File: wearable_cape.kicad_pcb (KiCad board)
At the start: 2 copper layers, 70.5 x 54.6 mm, 51 parts, among them P1 BELA_AINS, P2 RECEIVER, P3 BATTERY, P4 BELA_AOUTS, P5 CONN_01X04, P6 CONN_01X04, P7 CONN_01X04, SW1 SW_HALT, SW2 SW_MODE_SEL, U1 MCP6004, U2 MCP6004, U3 BEAGLEBONEBLACK, U4 OKI_7805

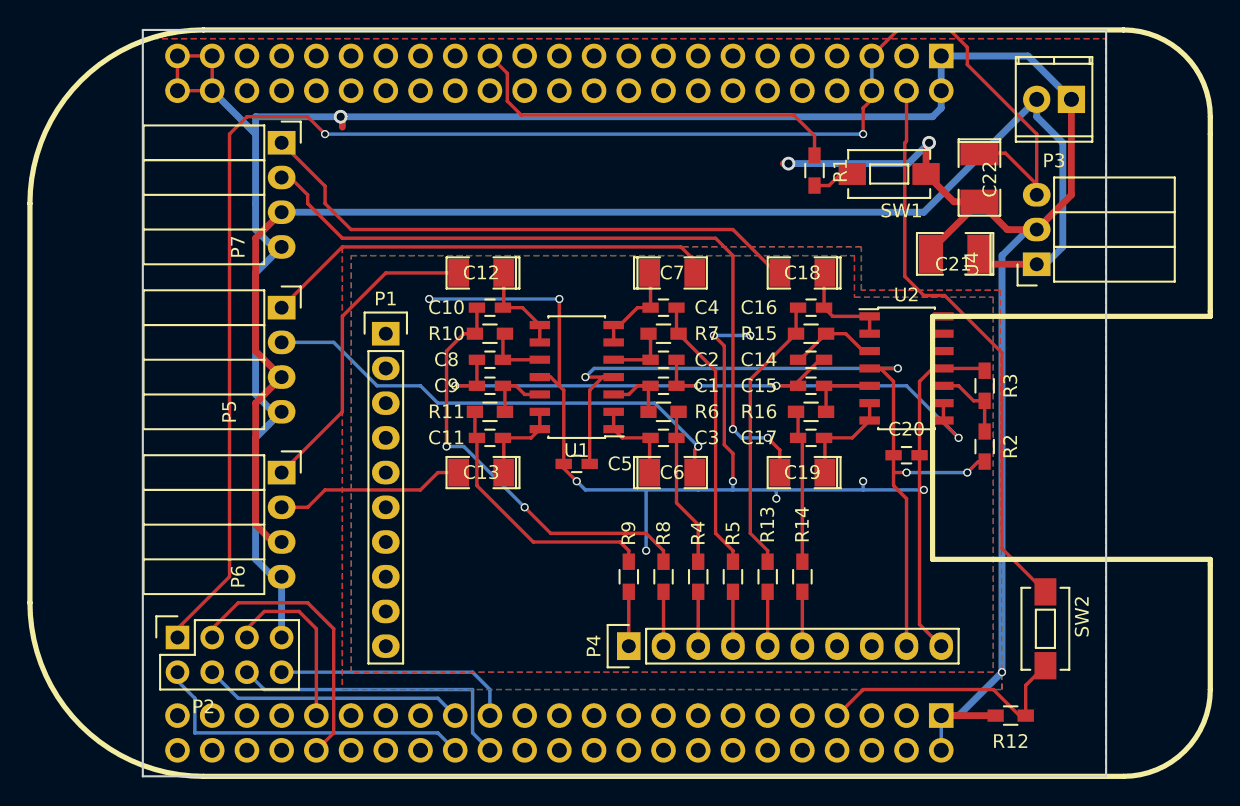
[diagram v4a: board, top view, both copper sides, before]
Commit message: updates to pcb: add attenuation, add headphone jacks, fix power supply opamps
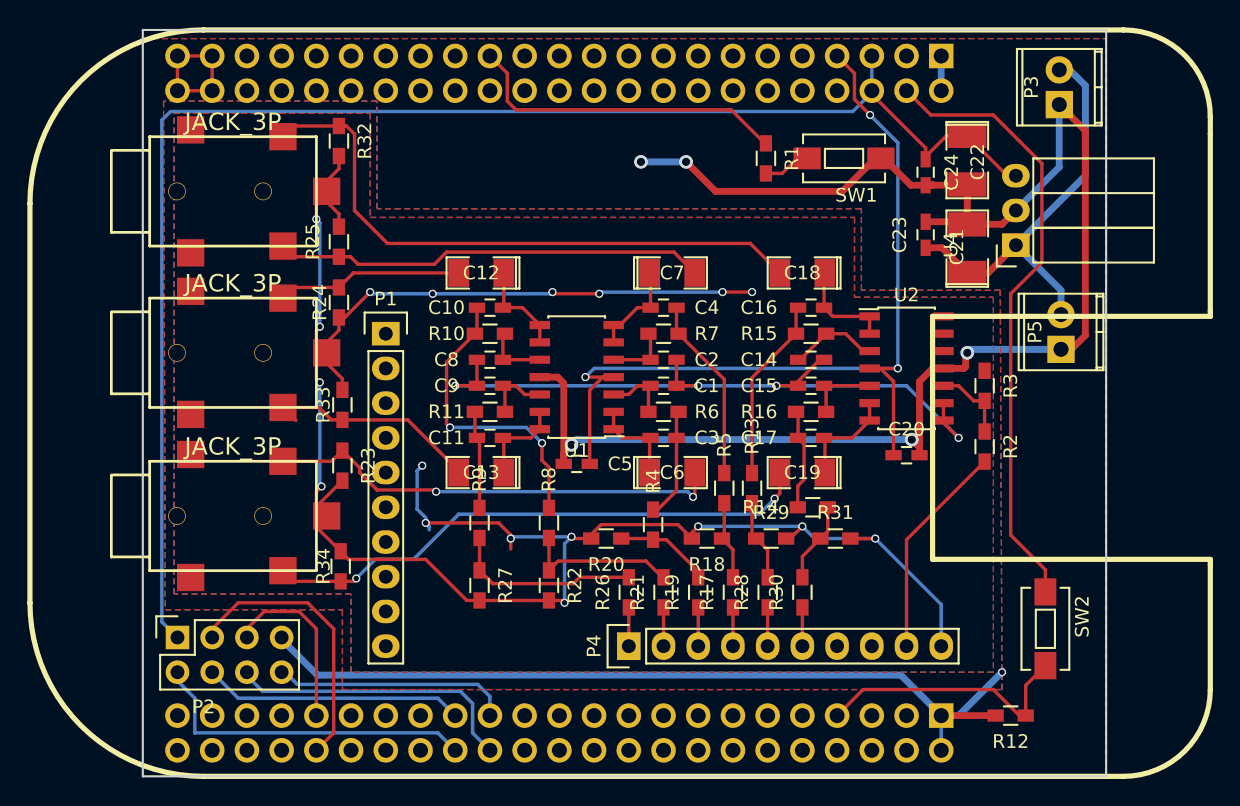
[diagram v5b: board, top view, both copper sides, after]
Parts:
- removed P6, P7: CONN_01X04, Socket_Strips:Socket_Strip_Angled_1x04
- added C23: C, Capacitors_SMD:C_0603_HandSoldering, F.Cu at (89.0, 33.4)
- added C24: C, Capacitors_SMD:C_0603_HandSoldering, F.Cu at (89.0, 28.8)
- added J1: JACK_3P, Lumberg:Lumberg_1503_03, F.Cu at (38.4, 54.0)
- added J2: JACK_3P, Lumberg:Lumberg_1503_03, F.Cu at (38.4, 42.0)
- added J3: JACK_3P, Lumberg:Lumberg_1503_03, F.Cu at (38.4, 30.2)
- added R17: 150k, Resistors_SMD:R_0603_HandSoldering, F.Cu at (74.9, 59.6)
- added R18: 200k, Resistors_SMD:R_0603_HandSoldering, F.Cu at (73.0, 55.6)
- added R19: 150k, Resistors_SMD:R_0603_HandSoldering, F.Cu at (72.4, 59.6)
- added R20: 200k, Resistors_SMD:R_0603_HandSoldering, F.Cu at (65.7, 55.6)
- added R21: 150k, Resistors_SMD:R_0603_HandSoldering, F.Cu at (69.8, 59.6)
- added R22: 200k, Resistors_SMD:R_0603_HandSoldering, F.Cu at (61.5, 59.1)
- added R23: 100k, Resistors_SMD:R_0603_HandSoldering, F.Cu at (46.4, 50.3)
- added R24: 100k, Resistors_SMD:R_0603_HandSoldering, F.Cu at (46.1, 38.4)
- added R25: 100k, Resistors_SMD:R_0603_HandSoldering, F.Cu at (46.1, 33.9)
- added R26: 150k, Resistors_SMD:R_0603_HandSoldering, F.Cu at (67.3, 59.6)
- added R27: 200k, Resistors_SMD:R_0603_HandSoldering, F.Cu at (56.4, 59.1)
- added R28: 150k, Resistors_SMD:R_0603_HandSoldering, F.Cu at (77.5, 59.6)
- added R29: 200k, Resistors_SMD:R_0603_HandSoldering, F.Cu at (77.7, 55.6)
- added R30: 150k, Resistors_SMD:R_0603_HandSoldering, F.Cu at (80.0, 59.6)
- added R31: 200k, Resistors_SMD:R_0603_HandSoldering, F.Cu at (82.4, 55.6)
- added R32: 100k, Resistors_SMD:R_0603_HandSoldering, F.Cu at (46.1, 26.5)
- added R33: 100k, Resistors_SMD:R_0603_HandSoldering, F.Cu at (46.4, 45.8)
- added R34: 100k, Resistors_SMD:R_0603_HandSoldering, F.Cu at (46.2, 57.7)
- P5: value CONN_01X04 -> PWR_OUT; footprint Socket_Strips:Socket_Strip_Angled_1x04 -> Terminal_Blocks:TerminalBlock_Pheonix_MPT-2.54mm_2pol
- moved P5 57.1 mm to (98.9, 41.8), turned to 90 degrees
- moved R9 11.6 mm to (56.4, 54.5)
- moved R8 9.26 mm to (61.5, 54.5)
- moved R13 6.58 mm to (76.3, 51.9)
- moved R5 6.51 mm to (74.3, 51.9)
- moved R14 5.14 mm to (80.8, 53.3), turned to 0 degrees
- moved R4 5.04 mm to (69.1, 54.6)
- moved R1 3.67 mm to (77.3, 27.8)
- moved SW1 3.49 mm to (83.1, 27.8)
- moved U4 2.07 mm to (95.6, 34.2)
- moved C22 1.55 mm to (92.1, 27.9)
- moved C21 0.97 mm to (92.1, 34.4), turned to 90 degrees
- moved P3 0.97 mm to (98.8, 23.9), turned to 90 degrees
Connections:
- C20 pad 1: VCC -> SYS_5V
- C20 pad 2: GNDA -> GND
- C5 pad 1: VCC -> SYS_5V
- C5 pad 2: GNDA -> GND
- P5 pad 1: /FILT_OUT1 -> GND
- P5 pad 2: /FILT_OUT0 -> BAT_11.1V
- R13 pad 2: /BELA_OUT4 -> Net-(R13-Pad2)
- R14 pad 2: /BELA_OUT5 -> Net-(R14-Pad2)
- R4 pad 2: /BELA_OUT2 -> Net-(R19-Pad2)
- R5 pad 2: /BELA_OUT3 -> Net-(R17-Pad2)
- R8 pad 2: /BELA_OUT1 -> Net-(R21-Pad2)
- R9 pad 2: /BELA_OUT0 -> Net-(R26-Pad2)
- U1 pad 11: GNDA -> GND
- U1 pad 4: VCC -> SYS_5V
- U2 pad 11: GNDA -> GND
- U2 pad 4: VCC -> SYS_5V
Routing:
- net BAT_11.1V: track 105.5 -> 30.8 mm
- net SYS_5V: track 0.00 -> 67.0 mm, vias 0 -> 3
- net GNDA: track 96.6 -> 153.7 mm, vias 10 -> 18
- net VCC: track 63.7 -> 15.9 mm, vias 4 -> 0
- net Net-(R26-Pad2): track 0.00 -> 13.9 mm
- net GND: track 209.7 -> 196.0 mm, vias 4 -> 6
- net /FILT_OUT5: track 54.2 -> 41.0 mm
- net Net-(C11-Pad2): track 19.3 -> 7.17 mm
- net Net-(R21-Pad2): track 0.00 -> 11.5 mm
- net RAW_5V: track 118.9 -> 109.1 mm, vias 2 -> 0
- net /FILT_OUT2: track 23.1 -> 13.6 mm
- net Net-(C10-Pad2): track 31.4 -> 21.9 mm
- net Net-(C16-Pad2): track 20.6 -> 13.5 mm
- net Net-(R19-Pad2): track 0.00 -> 7.05 mm
- net Net-(C4-Pad2): track 20.3 -> 13.6 mm
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
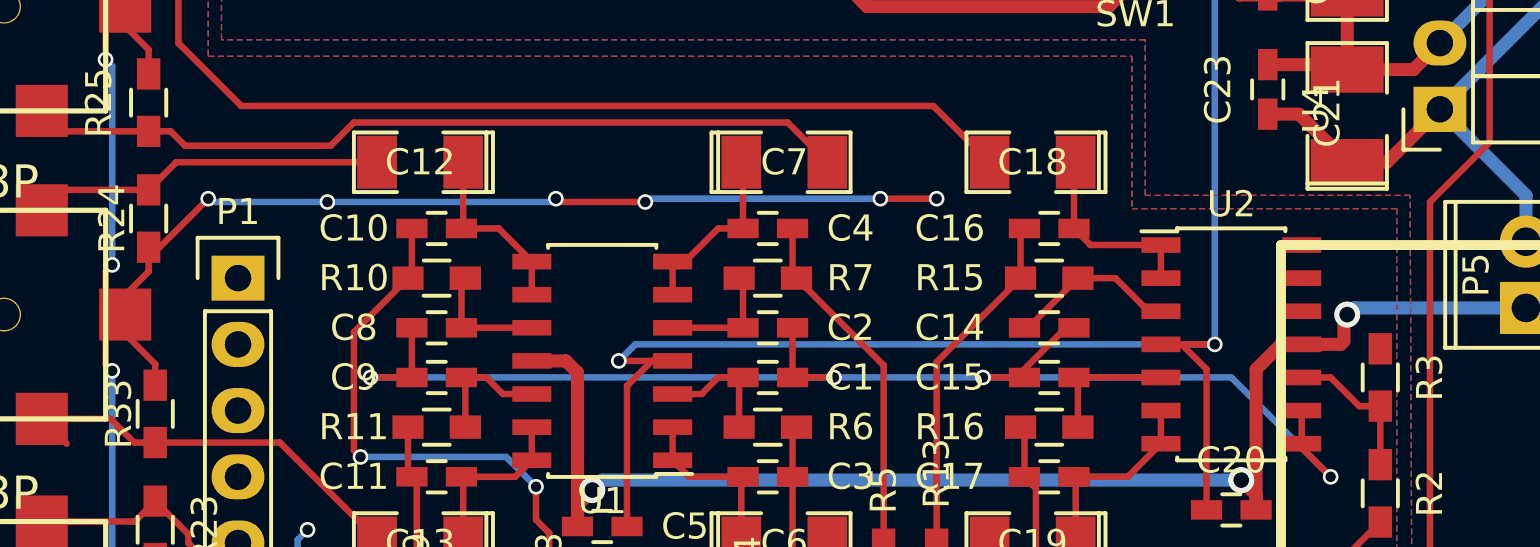
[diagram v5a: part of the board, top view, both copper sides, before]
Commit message: small update to pcb, updates to BOM
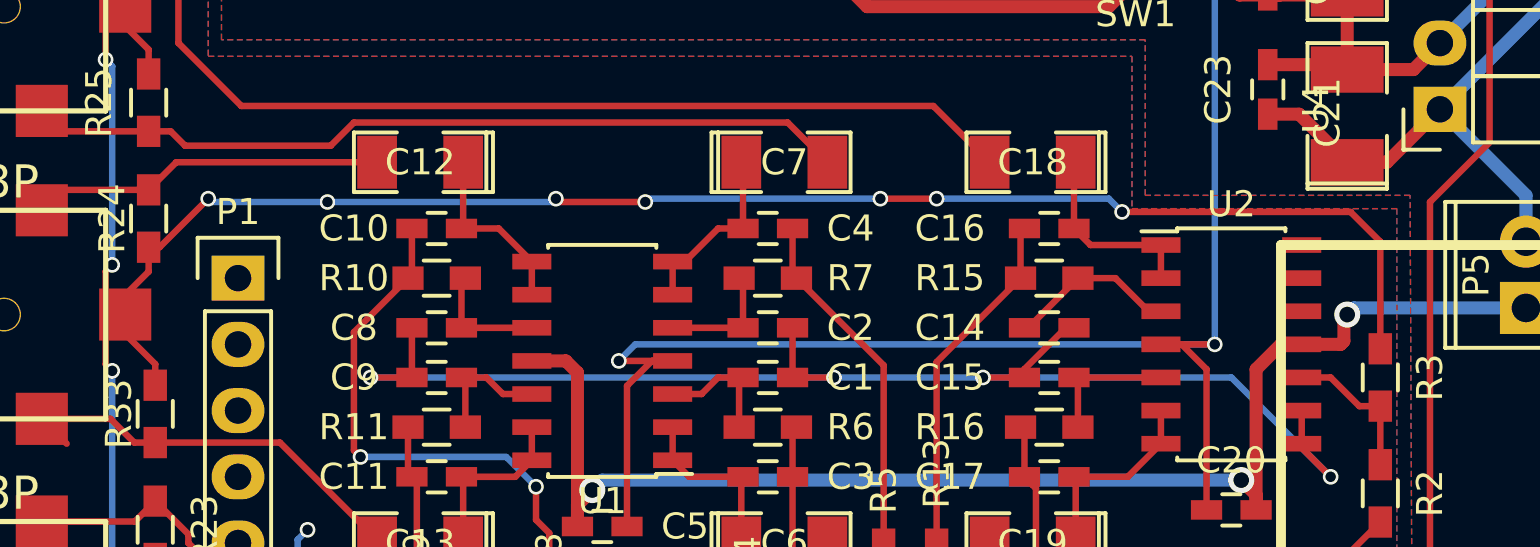
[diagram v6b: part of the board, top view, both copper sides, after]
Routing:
- net GNDA: track 153.7 -> 175.5 mm, vias 18 -> 19
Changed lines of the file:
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@@
   (general
     (links 143)
-    (no_connects 1)
-    (area 31.674999 18.339999 102.310001 73.100001)
+    (no_connects 0)
+    (area 23.004499 17.924499 110.345501 73.515501)
     (thickness 1.6)
     (drawings 4)
-    (tracks 464)
+    (tracks 470)
     (zones 0)
     (modules 72)
@@
   (segment (start 43.18 60.96) (end 44.45 62.23) (width 0.25) (layer F.Cu) (net 121))
   (segment (start 44.45 62.23) (end 44.45 68.58) (width 0.25) (layer F.Cu) (net 121))
-  (segment (start 52.959 37.719) (end 61.595 37.719) (width 0.25) (layer B.Cu) (net 122))
-  (via (at 48.387 37.592) (size 0.6) (drill 0.4) (layers F.Cu B.Cu) (net 122))
-  (segment (start 48.387 37.592) (end 48.514 37.719) (width 0.25) (layer B.Cu) (net 122))
-  (segment (start 48.514 37.719) (end 52.959 37.719) (width 0.25) (layer B.Cu) (net 122))
-  (via (at 52.959 37.719) (size 0.6) (drill 0.4) (layers F.Cu B.Cu) (net 122))
-  (segment (start 46.525 39.454) (end 48.387 37.592) (width 0.25) (layer F.Cu) (net 122))
-  (via (at 76.327 37.592) (size 0.6) (drill 0.4) (layers F.Cu B.Cu) (net 122))
-  (segment (start 74.168 37.592) (end 76.327 37.592) (width 0.25) (layer F.Cu) (net 122))
-  (via (at 74.168 37.592) (size 0.6) (drill 0.4) (layers F.Cu B.Cu) (net 122))
-  (segment (start 65.278 37.592) (end 74.168 37.592) (width 0.25) (layer B.Cu) (net 122))
-  (segment (start 65.151 37.719) (end 65.278 37.592) (width 0.25) (layer B.Cu) (net 122))
-  (via (at 65.151 37.719) (size 0.6) (drill 0.4) (layers F.Cu B.Cu) (net 122))
-  (segment (start 61.849 37.719) (end 65.151 37.719) (width 0.25) (layer F.Cu) (net 122))
-  (segment (start 61.722 37.592) (end 61.849 37.719) (width 0.25) (layer F.Cu) (net 122))
-  (via (at 61.722 37.592) (size 0.6) (drill 0.4) (layers F.Cu B.Cu) (net 122))
+  (segment (start 93.345 43.35) (end 93.345 39.243) (width 0.25) (layer F.Cu) (net 122) (status 400000))
   (segment (start 61.595 37.719) (end 61.722 37.592) (width 0.25) (layer B.Cu) (net 122))
+  (via (at 61.722 37.592) (size 0.6) (drill 0.4) (layers F.Cu B.Cu) (net 122))
+  (segment (start 61.722 37.592) (end 61.849 37.719) (width 0.25) (layer F.Cu) (net 122))
+  (segment (start 61.849 37.719) (end 65.151 37.719) (width 0.25) (layer F.Cu) (net 122))
+  (via (at 65.151 37.719) (size 0.6) (drill 0.4) (layers F.Cu B.Cu) (net 122))
+  (segment (start 65.151 37.719) (end 65.278 37.592) (width 0.25) (layer B.Cu) (net 122))
+  (segment (start 65.278 37.592) (end 74.168 37.592) (width 0.25) (layer B.Cu) (net 122))
+  (via (at 74.168 37.592) (size 0.6) (drill 0.4) (layers F.Cu B.Cu) (net 122))
+  (segment (start 74.168 37.592) (end 76.327 37.592) (width 0.25) (layer F.Cu) (net 122))
+  (via (at 76.327 37.592) (size 0.6) (drill 0.4) (layers F.Cu B.Cu) (net 122))
+  (segment (start 48.387 37.592) (end 46.525 39.454) (width 0.25) (layer F.Cu) (net 122))
+  (via (at 52.959 37.719) (size 0.6) (drill 0.4) (layers F.Cu B.Cu) (net 122))
+  (segment (start 48.514 37.719) (end 52.959 37.719) (width 0.25) (layer B.Cu) (net 122))
+  (segment (start 48.387 37.592) (end 48.514 37.719) (width 0.25) (layer B.Cu) (net 122))
+  (via (at 48.387 37.592) (size 0.6) (drill 0.4) (layers F.Cu B.Cu) (net 122))
+  (segment (start 52.959 37.719) (end 61.595 37.719) (width 0.25) (layer B.Cu) (net 122))
+  (segment (start 82.931 37.592) (end 76.327 37.592) (width 0.25) (layer B.Cu) (net 122))
+  (segment (start 83.439 38.1) (end 82.931 37.592) (width 0.25) (layer B.Cu) (net 122))
+  (via (at 83.439 38.1) (size 0.6) (drill 0.4) (layers F.Cu B.Cu) (net 122))
+  (segment (start 92.202 38.1) (end 83.439 38.1) (width 0.25) (layer F.Cu) (net 122))
+  (segment (start 93.345 39.243) (end 92.202 38.1) (width 0.25) (layer F.Cu) (net 122))
   (segment (start 46.101 39.454) (end 46.525 39.454) (width 0.25) (layer F.Cu) (net 122))
   (segment (start 52.451 54.483) (end 52.451 54.102) (width 0.25) (layer B.Cu) (net 122))
